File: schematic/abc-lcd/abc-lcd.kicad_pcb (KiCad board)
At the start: 2 copper layers, 39 parts, among them J1 24v-INPUT, J2 USB_A, J3 24v_OUTPUT, J4 ADJ_OUTPUT, Q1 IRFZ44, SW1 SW_Push, U1 74164, U2 RC1602A, U3 ATmega8A-PU, U4 LM2596S-5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

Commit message: Smaller version (not testerd yet)
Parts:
- moved J2 96.0 mm to (155.0, 120.3), turned to 90 degrees
- moved U4 75.8 mm to (90.0, 119.0), turned to 180 degrees
- moved R10 70.5 mm to (102.0, 114.0)
- moved RV1 49.5 mm to (154.7, 66.1)
- moved C6 49.4 mm to (130.0, 125.0)
- moved J3 48.5 mm to (156.5, 94.0)
- moved R11 48.5 mm to (129.9, 104.3)
- moved J4 48.2 mm to (156.3, 74.5)
- moved R12 47.7 mm to (146.9, 103.8)
- moved R5 47.5 mm to (146.8, 85.1), turned to 270 degrees
- moved SW1 43.2 mm to (71.0, 119.0), turned to 180 degrees
- moved R6 39.1 mm to (140.0, 86.1)
- moved R7 39.1 mm to (140.0, 91.1)
- moved R4 39.0 mm to (147.5, 115.0), turned to 180 degrees
- moved R13 37.4 mm to (78.0, 109.0), turned to 270 degrees
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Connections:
- U3 pad 18: (no net) -> BTN_SOURCE
- U3 pad 5: BTN_SOURCE -> (no net)
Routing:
- net GND_ENB: track 198.0 -> 123.5 mm
- net ADC_5V_0: track 327.7 -> 280.1 mm
- net ADC_ADJ_2: track 96.8 -> 55.7 mm
- net ADC_24V_4: track 86.6 -> 46.9 mm
- net BTN_SOURCE: track 60.3 -> 22.9 mm, vias 2 -> 0
- net v24: track 277.9 -> 243.0 mm, vias 0 -> 2
- net Net-(C7-Pad1): track 91.1 -> 59.1 mm
- net ADC_ADJS_3: track 121.9 -> 90.5 mm
- net GND: track 422.8 -> 393.4 mm
- net ADC_24S_5: track 108.9 -> 82.0 mm, vias 0 -> 2
- net Net-(RV1-Pad2): track 62.9 -> 46.5 mm
- net Net-(J2-Pad5): track 0.00 -> 13.1 mm
- net Net-(D1-Pad1): track 33.1 -> 21.0 mm
- net Net-(R2-Pad2): track 22.8 -> 12.5 mm
- net PWR_ENABLE: track 72.1 -> 62.3 mm, vias 0 -> 2
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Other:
- net class Default: clearance 0.6 -> 0.8; trace_width 0.6 -> 0.8; via_dia 0.6 -> 0.8
- net class pwr: via_dia 0.8 -> 1
- rule trace_clearance: 0.6 -> 0.8

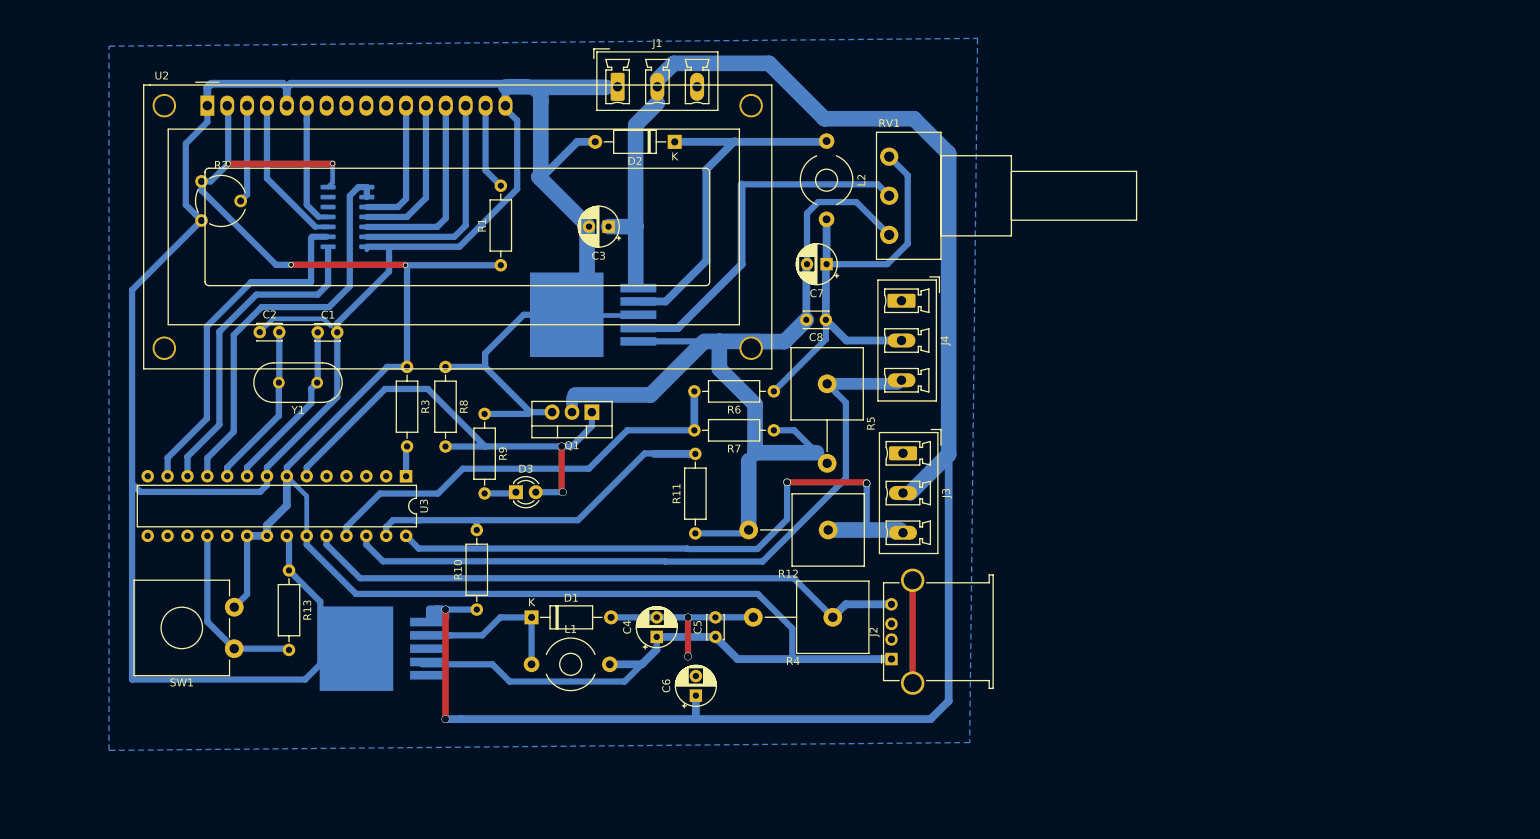
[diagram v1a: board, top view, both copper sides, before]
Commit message: Schematic with 2 missing capacitors (tested)
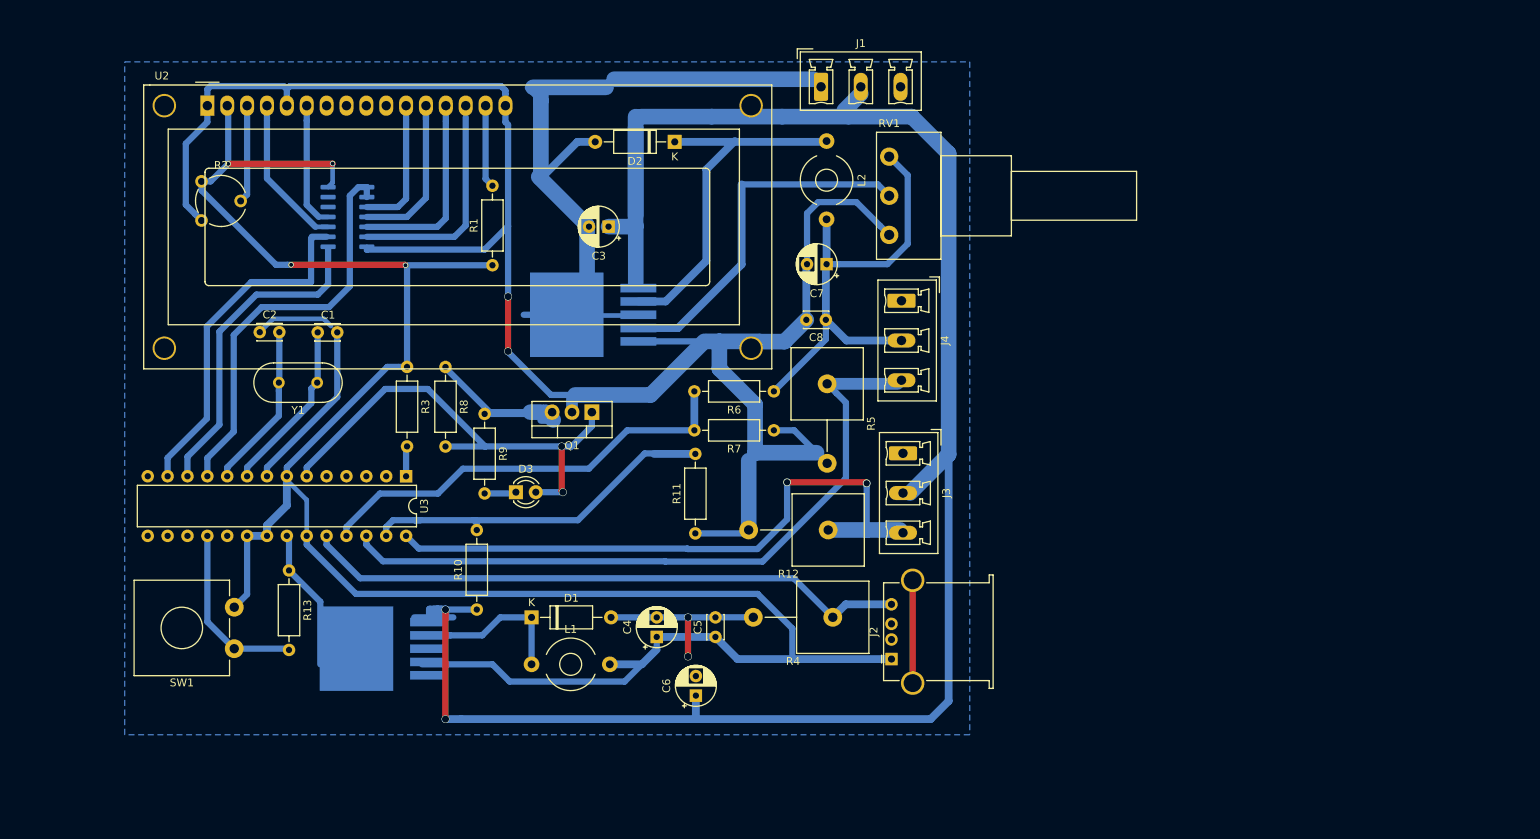
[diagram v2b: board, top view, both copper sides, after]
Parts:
- moved J1 26.0 mm to (146.0, 47.2)
- moved R1 1.07 mm to (104.0, 70.0)
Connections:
- R2 pad 1: GND -> GND_ENB
- U1 pad 7: GND -> GND_ENB
- U2 pad : (no net) -> GND_ENB
- U2 pad 1: GND -> GND_ENB
- U2 pad 16: GND -> GND_ENB
- U2 pad 5: GND -> GND_ENB
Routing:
- net GND: track 393.4 -> 197.0 mm
- net GND_ENB: track 123.5 -> 247.7 mm, vias 0 -> 2
- net v24: track 243.0 -> 258.2 mm
- net ADC_5V_0: track 280.1 -> 279.0 mm
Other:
- net class Default: via_dia 0.8 -> 0.5
- net class pwr: via_drill 0.4 -> 0.8
